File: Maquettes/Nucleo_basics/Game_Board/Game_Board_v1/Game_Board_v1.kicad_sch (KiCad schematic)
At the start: 42 parts, among them CON1 MikroE-nRF-S-module, J1 TFT-RB1.8, J2 JOYSTICK, J3 AnalogIn, J4 AnalogChoice, SW1 SW_Push, SW2 SW_Push, SW3 SW_Push, SW4 SW_Push, U1 NUCLEO-L432KC, U2 MCP23008-xP, U3 4071

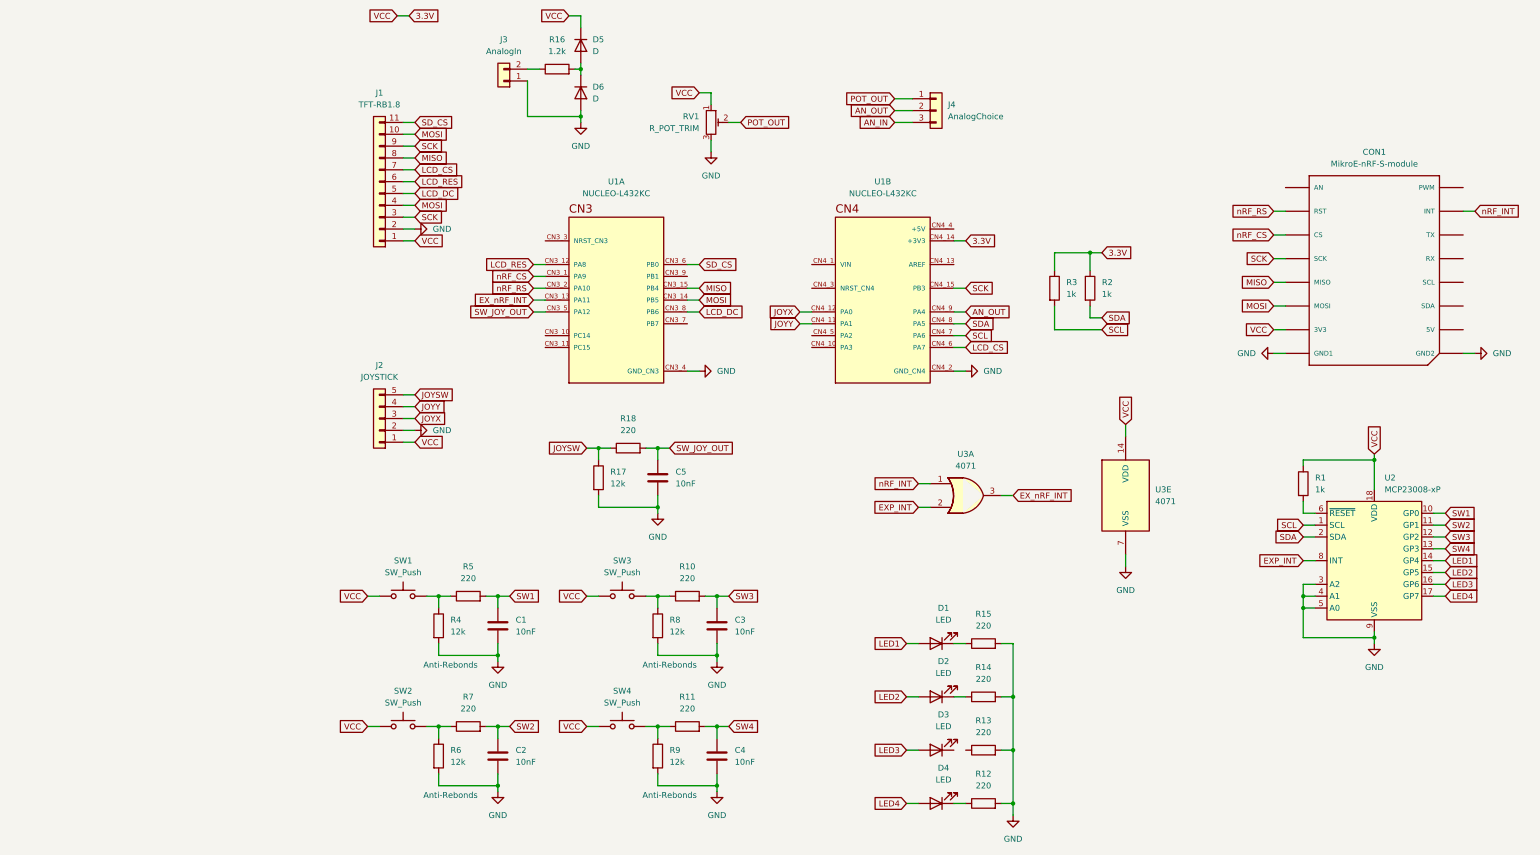
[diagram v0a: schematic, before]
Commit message: GameBoard NucleoBasics update
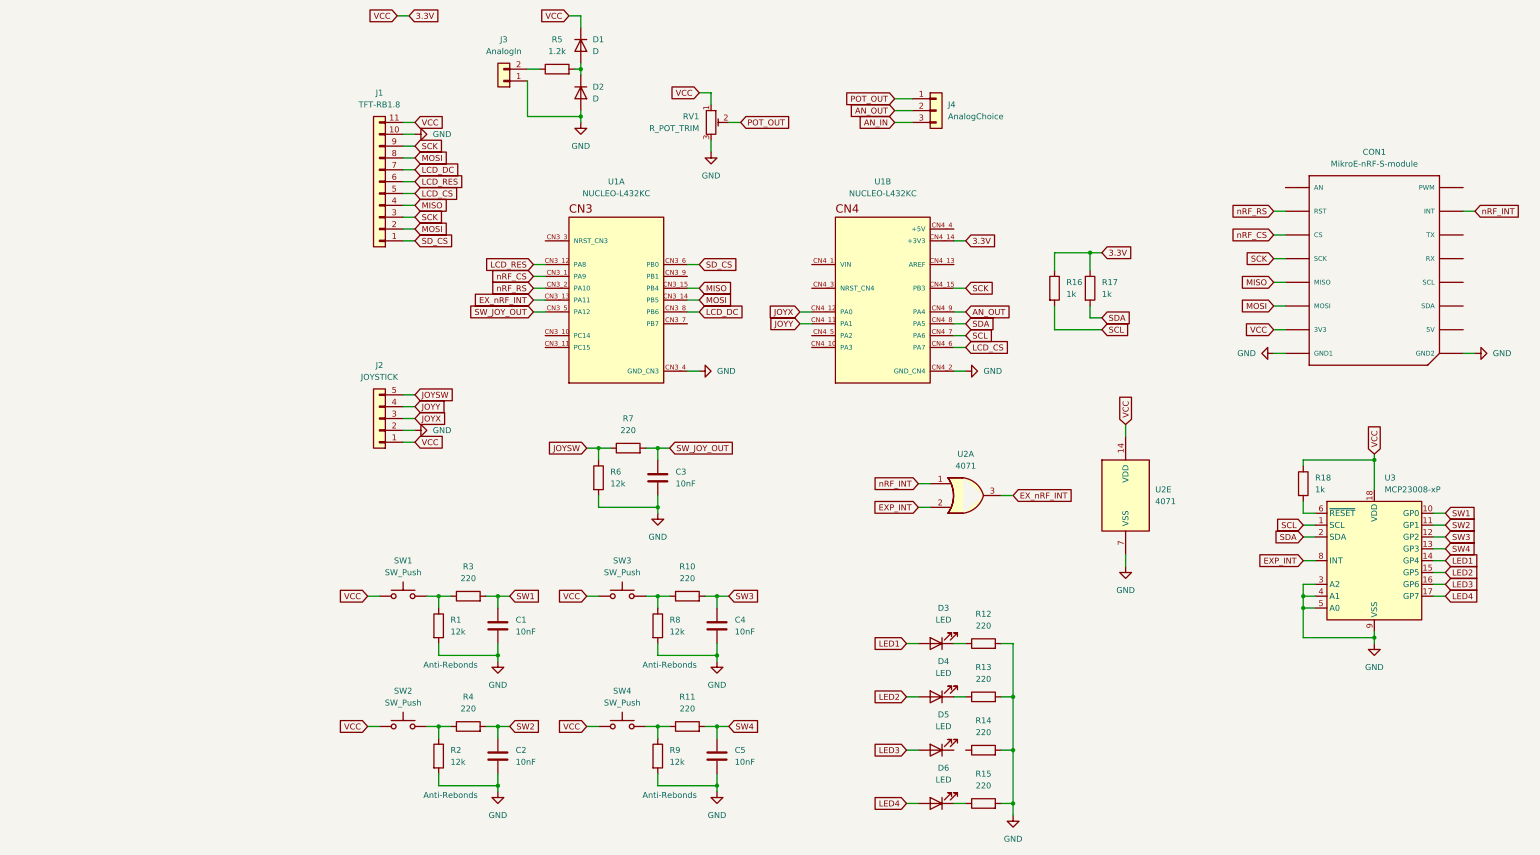
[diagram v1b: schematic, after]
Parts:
- C1, C2: footprint (none) -> Capacitor_THT:C_Rect_L7.0mm_W3.5mm_P5.00mm
- C3: renamed from C5; footprint (none) -> Capacitor_THT:C_Rect_L7.0mm_W3.5mm_P5.00mm
- C4: renamed from C3; footprint (none) -> Capacitor_THT:C_Rect_L7.0mm_W3.5mm_P5.00mm
- C5: renamed from C4; footprint (none) -> Capacitor_THT:C_Rect_L7.0mm_W3.5mm_P5.00mm
- CON1: footprint MIKROBUS_MODULE_CONN -> mikroBUS:MIKROBUS_HOST_CONN
- D1: renamed from D5; footprint (none) -> Diode_THT:D_DO-35_SOD27_P7.62mm_Horizontal
- D2: renamed from D6; footprint (none) -> Diode_THT:D_DO-35_SOD27_P7.62mm_Horizontal
- D3: renamed from D1; footprint (none) -> LED_THT:LED_D3.0mm_Clear
- D4: renamed from D2; footprint (none) -> LED_THT:LED_D3.0mm_Clear
- D5: renamed from D3; footprint (none) -> LED_THT:LED_D3.0mm_Clear
- D6: renamed from D4; footprint (none) -> LED_THT:LED_D3.0mm_Clear
- J1: footprint (none) -> Connector_PinSocket_2.54mm:PinSocket_1x11_P2.54mm_Horizontal
- J2: footprint (none) -> Connector_PinSocket_2.54mm:PinSocket_1x05_P2.54mm_Horizontal
- J3: footprint (none) -> Connector_PinSocket_2.54mm:PinSocket_1x02_P2.54mm_Horizontal
- J4: footprint (none) -> Connector_PinHeader_2.54mm:PinHeader_1x03_P2.54mm_Horizontal
- R1: renamed from R4; footprint (none) -> Resistor_THT:R_Axial_DIN0207_L6.3mm_D2.5mm_P10.16mm_Horizontal
- R10, R11, R8, R9: footprint (none) -> Resistor_THT:R_Axial_DIN0207_L6.3mm_D2.5mm_P10.16mm_Horizontal
- R12: renamed from R15; footprint (none) -> Resistor_THT:R_Axial_DIN0207_L6.3mm_D2.5mm_P10.16mm_Horizontal
- R13: renamed from R14; footprint (none) -> Resistor_THT:R_Axial_DIN0207_L6.3mm_D2.5mm_P10.16mm_Horizontal
- R14: renamed from R13; footprint (none) -> Resistor_THT:R_Axial_DIN0207_L6.3mm_D2.5mm_P10.16mm_Horizontal
- R15: renamed from R12; footprint (none) -> Resistor_THT:R_Axial_DIN0207_L6.3mm_D2.5mm_P10.16mm_Horizontal
- R16: renamed from R3; footprint (none) -> Resistor_THT:R_Axial_DIN0207_L6.3mm_D2.5mm_P10.16mm_Horizontal
- R17: renamed from R2; footprint (none) -> Resistor_THT:R_Axial_DIN0207_L6.3mm_D2.5mm_P10.16mm_Horizontal
- R18: renamed from R1; footprint (none) -> Resistor_THT:R_Axial_DIN0207_L6.3mm_D2.5mm_P10.16mm_Horizontal
- R2: renamed from R6; footprint (none) -> Resistor_THT:R_Axial_DIN0207_L6.3mm_D2.5mm_P10.16mm_Horizontal
- R3: renamed from R5; footprint (none) -> Resistor_THT:R_Axial_DIN0207_L6.3mm_D2.5mm_P10.16mm_Horizontal
- R4: renamed from R7; footprint (none) -> Resistor_THT:R_Axial_DIN0207_L6.3mm_D2.5mm_P10.16mm_Horizontal
- R5: renamed from R16; footprint (none) -> Resistor_THT:R_Axial_DIN0207_L6.3mm_D2.5mm_P10.16mm_Horizontal
- R6: renamed from R17; footprint (none) -> Resistor_THT:R_Axial_DIN0207_L6.3mm_D2.5mm_P10.16mm_Horizontal
- R7: renamed from R18; footprint (none) -> Resistor_THT:R_Axial_DIN0207_L6.3mm_D2.5mm_P10.16mm_Horizontal
- RV1: footprint (none) -> Potentiometer_THT:Potentiometer_Vishay_T73YP_Vertical
- SW1, SW2, SW3, SW4: footprint (none) -> Resistor_THT:R_Axial_DIN0207_L6.3mm_D2.5mm_P5.08mm_Vertical
- U1: footprint NUCLEO-L432KC:MODULE_NUCLEO-L432KC -> NUCLEO_L432KC:MODULE_NUCLEO-L432KC
- U2: renamed from U3; footprint (none) -> Package_DIP:DIP-14_W7.62mm_Socket_LongPads
- renumbered U2 to U3
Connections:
- net 3.3V: now also J1.11 (Pin_11); no longer J1.1 (Pin_1)
- net GND: now also J1.10 (Pin_10); no longer J1.2 (Pin_2)
- net LCD_CS: now also J1.5 (Pin_5); no longer J1.7 (Pin_7)
- net LCD_DC: now also J1.7 (Pin_7); no longer J1.5 (Pin_5)
- net MISO: now also J1.4 (Pin_4); no longer J1.8 (Pin_8)
- net MOSI: now also J1.2 (Pin_2), J1.8 (Pin_8); no longer J1.10 (Pin_10), J1.4 (Pin_4)
- net SD_CS: now also J1.1 (Pin_1); no longer J1.11 (Pin_11)

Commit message: Update GameBoard
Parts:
- removed R10, R11, R3, R7: 220, Resistor_THT:R_Axial_DIN0207_L6.3mm_D2.5mm_P10.16mm_Horizontal, symbol Device:R
- removed R8, R9: 12k, Resistor_THT:R_Axial_DIN0207_L6.3mm_D2.5mm_P10.16mm_Horizontal, symbol Device:R
- removed unit 1 of U2
- added J5: Conn_01x02, TerminalBlock_Phoenix:TerminalBlock_Phoenix_PT-1,5-2-5.0-H_1x02_P5.00mm_Horizontal, symbol Connector_Generic:Conn_01x02
- added J6: Conn_01x04, Connector_PinHeader_2.54mm:PinHeader_1x04_P2.54mm_Horizontal, symbol Connector_Generic:Conn_01x04
- added R5: 12k, Resistor_THT:R_Axial_DIN0207_L6.3mm_D2.5mm_P10.16mm_Horizontal, symbol Device:R
- added unit 3 of U2
- R4: value 220 -> 12k
- RV1: value R_POT_TRIM -> R_10k
- SW1, SW2, SW3, SW4: footprint Resistor_THT:R_Axial_DIN0207_L6.3mm_D2.5mm_P5.08mm_Vertical -> LEnsE_devices:Switch
- renumbered R15 to R10, R16 to R11, R17 to R12, R18 to R13, R5 to R3, R12 to R7, R13 to R8, R14 to R9
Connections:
- net 3.3V: now also C1.1, C2.1, C3.1, C4.1, C5.1
- net AN_IN: now also D1.2 (A), D2.1 (K), R3.2
- net EXP_INT: now also U2.9
- net EX_nRF_INT: now also U2.10
- net GND: now also R4.2, J5.1 (Pin_1), J6.4 (Pin_4), R5.2; no longer C1.2, C2.2, C3.2, C4.2, C5.2
- net JOYSW: now also C5.2, U1.CN3_5 (PA12)
- net LCD_DC: now also U1.CN3_9 (PB1); no longer U1.CN3_8 (PB6)
- net SCL: now also U1.CN3_8 (PB6), J6.1 (Pin_1); no longer U1.CN4_7 (PA6)
- net SDA: now also U1.CN3_7 (PB7), J6.2 (Pin_2); no longer U1.CN4_8 (PA5)
- net SW1: now also C1.2, R1.1, SW1.2; no longer C1.1
- net SW2: now also C2.2, R2.1, SW2.2; no longer C2.1, R4.2
- net SW3: now also C3.2, R4.1, SW3.2; no longer C4.1
- net SW4: now also C4.2, SW4.2, R5.1; no longer C5.1
- net nRF_INT: now also U2.8
- net Vin: now reaches U1.CN4_1 (VIN)
- net Vin: now also J5.2 (Pin_2)
- net 5V: now reaches U1.CN4_4 (+5V)
- net 5V: now also J6.3 (Pin_3)
- net at R9.1: now also D5.1 (K)
- removed net SW_JOY_OUT: C3.1, U1.CN3_5 (PA12)
- no-connect marks 0 -> 7
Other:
- moved on the sheet: C1, J3

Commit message: Update GameBoard
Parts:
- added J10: nRF_temp1, Connector_PinSocket_2.54mm:PinSocket_1x02_P2.54mm_Vertical, symbol Connector_Generic:Conn_01x02
- added J11: nRF_temp2, Connector_PinSocket_2.54mm:PinSocket_1x02_P2.54mm_Vertical, symbol Connector_Generic:Conn_01x02
- added J7: LCD_TEMp, Connector_PinSocket_2.54mm:PinSocket_1x03_P2.54mm_Vertical, symbol Connector_Generic:Conn_01x03
- added J8, J9: SD_CS_t1, Connector_PinSocket_2.54mm:PinSocket_1x01_P2.54mm_Vertical, symbol Connector_Generic:Conn_01x01
- R10, R7, R8, R9: value 220 -> 100
- R11, R12, R13: value 1k -> 680
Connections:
- net AN_OUT: now also U1.CN4_6 (PA7); no longer U1.CN4_9 (PA4)
- net EXP_INT: now also U2.13; no longer U2.9
- net EX_nRF_INT: now also U1.CN3_5 (PA12), U2.11; no longer U1.CN3_13 (PA11), U2.10
- net JOYSW: now also U1.CN4_9 (PA4); no longer U1.CN3_5 (PA12)
- net LCD_CS: no longer U1.CN4_6 (PA7)
- net LCD_DC: no longer U1.CN3_9 (PB1)
- net LCD_RES: no longer U1.CN3_12 (PA8)
- net SD_CS: now also J8.1 (Pin_1); no longer U1.CN3_6 (PB0)
- net nRF_CS: now also J11.2 (Pin_2); no longer U1.CN3_1 (PA9)
- net nRF_INT: now also U2.12; no longer U2.8
- net nRF_RS: now also J11.1 (Pin_1); no longer U1.CN3_2 (PA10)
- new net LCD_CS_t: J7.3 (Pin_3), U1.CN3_13 (PA11)
- new net LCD_DC_t: J7.1 (Pin_1), U1.CN3_9 (PB1)
- new net LCD_RES_t: J7.2 (Pin_2), U1.CN3_12 (PA8)
- new net SD_CS_t: J9.1 (Pin_1), U1.CN3_6 (PB0)
- new net nRF_CS_t: J10.1 (Pin_1), U1.CN3_1 (PA9)
- new net nRF_RS_t: J10.2 (Pin_2), U1.CN3_2 (PA10)

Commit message: Create DemoBoard PhD/LED
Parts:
- J6: value Conn_01x04 -> I2C_EXT
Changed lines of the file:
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@@
 			)
 		)
-		(property "Value" "Conn_01x04"
+		(property "Value" "I2C_EXT"
 			(at 191.77 49.5299 0)
 			(effects

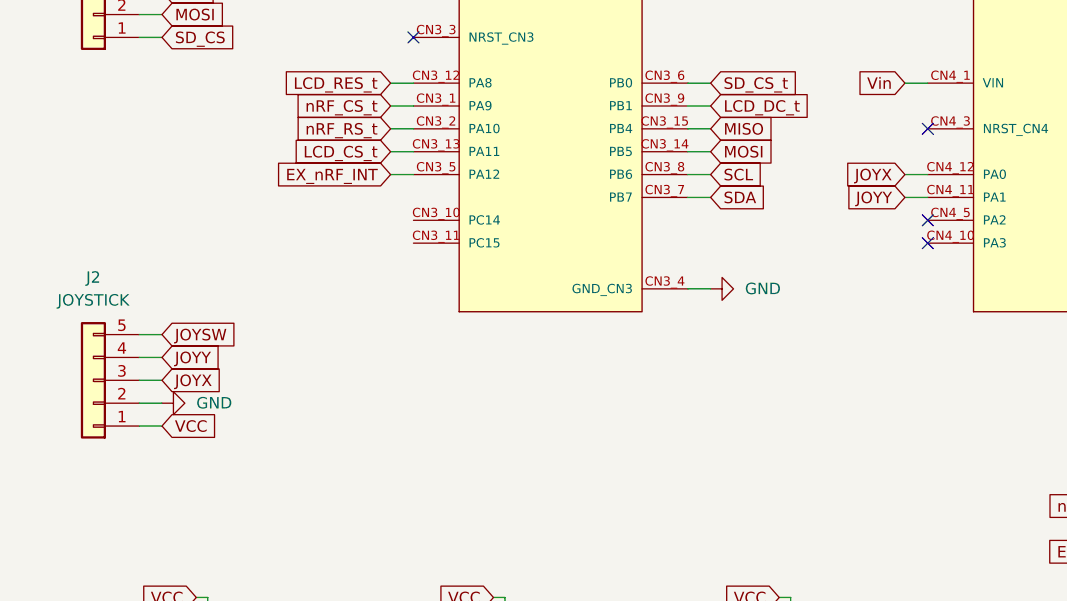
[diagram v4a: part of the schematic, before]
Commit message: Update Gameboard
Change Joystick connector !!
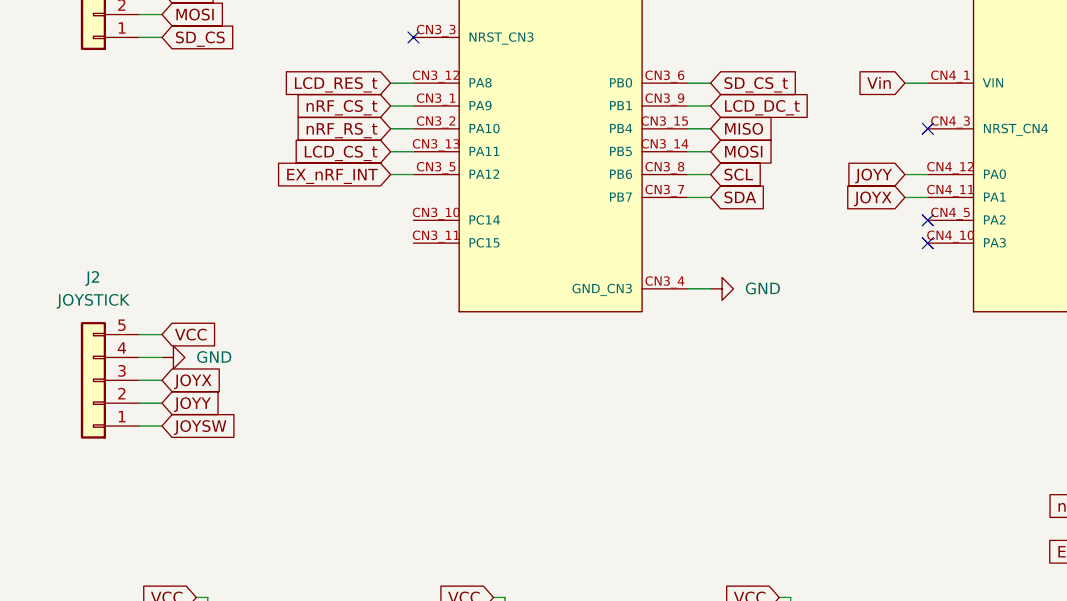
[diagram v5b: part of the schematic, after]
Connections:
- net 3.3V: now also J2.5 (Pin_5); no longer J2.1 (Pin_1)
- net GND: now also J2.4 (Pin_4); no longer J2.2 (Pin_2)
- net JOYSW: now also J2.1 (Pin_1); no longer J2.5 (Pin_5)
- net JOYX: now also U1.CN4_11 (PA1); no longer U1.CN4_12 (PA0)
- net JOYY: now also J2.2 (Pin_2), U1.CN4_12 (PA0); no longer J2.4 (Pin_4), U1.CN4_11 (PA1)
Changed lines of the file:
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@@
 	(global_label "VCC"
 		(shape input)
-		(at 35.56 107.95 0)
+		(at 35.56 97.79 0)
 		(fields_autoplaced yes)
 		(effects
@@
 		)
 		(property "Intersheetrefs" "${INTERSHEET_REFS}"
-			(at 42.1738 107.95 0)
+			(at 42.1738 97.79 0)
 			(effects
 				(font
@@
 	(global_label "JOYY"
 		(shape input)
-		(at 118.11 82.55 180)
+		(at 118.11 80.01 180)
 		(fields_autoplaced yes)
 		(effects
@@
 		)
 		(property "Intersheetrefs" "${INTERSHEET_REFS}"
-			(at 110.6495 82.55 0)
+			(at 110.6495 80.01 0)
 			(effects
 				(font
@@
 	(global_label "JOYY"
 		(shape input)
-		(at 35.56 100.33 0)
+		(at 35.56 105.41 0)
 		(fields_autoplaced yes)
 		(effects
@@
 		)
 		(property "Intersheetrefs" "${INTERSHEET_REFS}"
-			(at 43.0205 100.33 0)
+			(at 43.0205 105.41 0)
 			(effects
 				(font
@@
 	(global_label "JOYX"
 		(shape input)
-		(at 118.11 80.01 180)
+		(at 118.11 82.55 180)
 		(fields_autoplaced yes)
 		(effects
@@
 		)
 		(property "Intersheetrefs" "${INTERSHEET_REFS}"
-			(at 110.5286 80.01 0)
+			(at 110.5286 82.55 0)
 			(effects
 				(font
@@
 	(global_label "JOYSW"
 		(shape input)
-		(at 35.56 97.79 0)
+		(at 35.56 107.95 0)
 		(fields_autoplaced yes)
 		(effects
@@
 		)
 		(property "Intersheetrefs" "${INTERSHEET_REFS}"
-			(at 44.5928 97.79 0)
+			(at 44.5928 107.95 0)
 			(effects
 				(font
@@
 	(symbol
 		(lib_id "power:GND")
-		(at 35.56 105.41 90)
+		(at 35.56 100.33 90)
 		(unit 1)
 		(exclude_from_sim no)
@@
 		(fields_autoplaced yes)
 		(property "Reference" "#PWR02"
-			(at 41.91 105.41 0)
+			(at 41.91 100.33 0)
 			(effects
 				(font
@@
 		)
 		(property "Value" "GND"
-			(at 39.37 105.4099 90)
+			(at 39.37 100.3299 90)
 			(effects
 				(font
@@
 		)
 		(property "Footprint" ""
-			(at 35.56 105.41 0)
+			(at 35.56 100.33 0)
 			(effects
 				(font
@@
 		)
 		(property "Datasheet" ""
-			(at 35.56 105.41 0)
+			(at 35.56 100.33 0)
 			(effects
 				(font
@@
 		)
 		(property "Description" "Power symbol creates a global label with name \"GND\" , ground"
-			(at 35.56 105.41 0)
+			(at 35.56 100.33 0)
 			(effects
 				(font

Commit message: Update GameBoard
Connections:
- net nRF_RS renamed nRF_CE
- net nRF_RS_t renamed nRF_CE_t
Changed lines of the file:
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@@
 		)
 	)
-	(global_label "nRF_RS_t"
+	(global_label "nRF_CE_t"
 		(shape input)
 		(at -34.29 87.63 180)
@@
 		)
 		(property "Intersheetrefs" "${INTERSHEET_REFS}"
-			(at -45.9232 87.63 0)
+			(at -45.8627 87.63 0)
 			(effects
 				(font
@@
 		)
 	)
-	(global_label "nRF_RS_t"
+	(global_label "nRF_CE_t"
 		(shape input)
 		(at 60.96 74.93 180)
@@
 		)
 		(property "Intersheetrefs" "${INTERSHEET_REFS}"
-			(at 49.3268 74.93 0)
+			(at 49.3873 74.93 0)
 			(effects
 				(font
@@
 		)
 	)
-	(global_label "nRF_RS"
+	(global_label "nRF_CE"
 		(shape input)
 		(at -34.29 95.25 180)
@@
 		)
 		(property "Intersheetrefs" "${INTERSHEET_REFS}"
-			(at -44.2299 95.25 0)
+			(at -44.1694 95.25 0)
 			(effects
 				(font
@@
 		)
 	)
-	(global_label "nRF_RS"
+	(global_label "nRF_CE"
 		(shape input)
 		(at 219.71 58.42 180)
@@
 		)
 		(property "Intersheetrefs" "${INTERSHEET_REFS}"
-			(at 209.7701 58.42 0)
-			(effects
-				(font
+			(at 209.8306 58.42 0)
+			(effects
+				(font
